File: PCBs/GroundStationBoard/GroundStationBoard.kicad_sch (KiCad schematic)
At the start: 4 parts, among them J1 SMA_CONNECTOR, U1 RFM98W

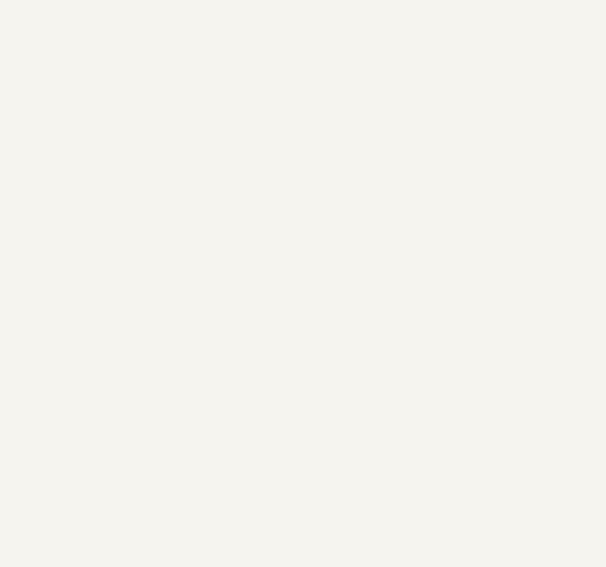
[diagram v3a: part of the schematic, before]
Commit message: added amplifier
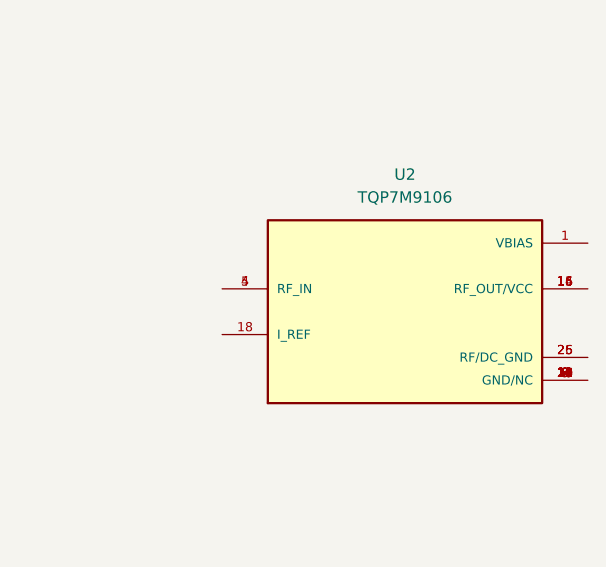
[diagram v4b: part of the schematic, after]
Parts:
- added U2: TQP7M9106, TQP7M9106:QFN50P400X400X90-25N, symbol TQP7M9106:TQP7M9106
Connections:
- new net: U2.10 (GND/NC), U2.11 (GND/NC), U2.12 (GND/NC), U2.13 (GND/NC), U2.17 (GND/NC), U2.19 (GND/NC), U2.2 (GND/NC), U2.20 (GND/NC), U2.21 (GND/NC), U2.22 (GND/NC), U2.23 (GND/NC), U2.24 (GND/NC), U2.3 (GND/NC), U2.6 (GND/NC), U2.7 (GND/NC), U2.8 (GND/NC), U2.9 (GND/NC)
- new net: U2.14 (RF_OUT/VCC), U2.15 (RF_OUT/VCC), U2.16 (RF_OUT/VCC)
- new net: U2.25 (RF/DC_GND), U2.26 (RF/DC_GND)
- new net: U2.4 (RF_IN), U2.5 (RF_IN)
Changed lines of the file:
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@@
     (pin "1")
+  )
+  (symbol (lib_id "TQP7M9106:TQP7M9106") (at 234.95 95.25 0) (unit 1)
+    (in_bom yes) (on_board yes) (fields_autoplaced)
+    (property "Reference" "U2" (id 0) (at 234.95 80.01 0))
+    (property "Value" "TQP7M9106" (id 1) (at 234.95 82.55 0))
+    (property "Footprint" "TQP7M9106:QFN50P400X400X90-25N" (id 2) (at 234.95 95.25 0)
+      (effects (font (size 1.27 1.27)) (justify left bottom) hide)
+    )
+    (property "Datasheet" "" (id 3) (at 234.95 95.25 0)
+      (effects (font (size 1.27 1.27)) (justify left bottom) hide)
+    )
+    (property "MANUFACTURER" "Qorvo" (id 4) (at 234.95 95.25 0)
+      (effects (font (size 1.27 1.27)) (justify left bottom) hide)
+    )
+    (property "STANDARD" "IPC-7351B" (id 5) (at 234.95 95.25 0)
+      (effects (font (size 1.27 1.27)) (justify left bottom) hide)
+    )
+    (property "SNAPEDA_PN" "TQP7M9106" (id 6) (at 234.95 95.25 0)
+      (effects (font (size 1.27 1.27)) (justify left bottom) hide)
+    )
+    (property "PARTREV" "Rev.D" (id 7) (at 234.95 95.25 0)
+      (effects (font (size 1.27 1.27)) (justify left bottom) hide)
+    )
+    (property "MAXIMUM_PACKAGE_HEIGHT" "0.9 mm" (id 8) (at 234.95 95.25 0)
+      (effects (font (size 1.27 1.27)) (justify left bottom) hide)
+    )
+    (pin "1")
+    (pin "10")
+    (pin "11")
+    (pin "12")
+    (pin "13")
+    (pin "14")
+    (pin "15")
+    (pin "16")
+    (pin "17")
+    (pin "18")
+    (pin "19")
+    (pin "2")
+    (pin "20")
+    (pin "21")
+    (pin "22")
+    (pin "23")
+    (pin "24")
+    (pin "25")
+    (pin "26")
+    (pin "3")
+    (pin "4")
+    (pin "5")
+    (pin "6")
+    (pin "7")
+    (pin "8")
+    (pin "9")
   )
   (symbol (lib_id "power:GND") (at 111.76 63.5 0) (unit 1)
@@
   (symbol (lib_id "power:GND") (at 152.4 114.3 0) (unit 1)
     (in_bom yes) (on_board yes)
-    (property "Reference" "#PWR016" (id 0) (at 152.4 120.65 0)
+    (property "Reference" "#PWR013" (id 0) (at 152.4 120.65 0)
       (effects (font (size 1.27 1.27)) hide)
     )
@@
       (reference "#PWR012") (unit 1) (value "GND") (footprint "")
     )
+    (path "/d773327a-e8d6-4108-a114-a6c62372afcb"
+      (reference "#PWR013") (unit 1) (value "GND") (footprint "")
+    )
     (path "/df933423-8150-4da9-a8c1-053c01a26516"
       (reference "#PWR014") (unit 1) (value "+3.3V") (footprint "")
@@
       (reference "#PWR015") (unit 1) (value "GND") (footprint "")
     )
-    (path "/d773327a-e8d6-4108-a114-a6c62372afcb"
-      (reference "#PWR016") (unit 1) (value "GND") (footprint "")
-    )
     (path "/695f3645-22ae-40bc-a3f8-3d3b654779fc"
       (reference "A1") (unit 1) (value "Raspberry Pi Zero") (footprint "ADA3708:ADA3708_RPI-ZERO")
@@
       (reference "U1") (unit 1) (value "RFM98W") (footprint "RFM98W-433S2:XCVR_RFM98W-433S2")
     )
-  )
+    (path "/6e9a568d-d4c1-4c8f-ab20-c2e09c01ec01"
+      (reference "U2") (unit 1) (value "TQP7M9106") (footprint "TQP7M9106:QFN50P400X400X90-25N")
+    )
+  )

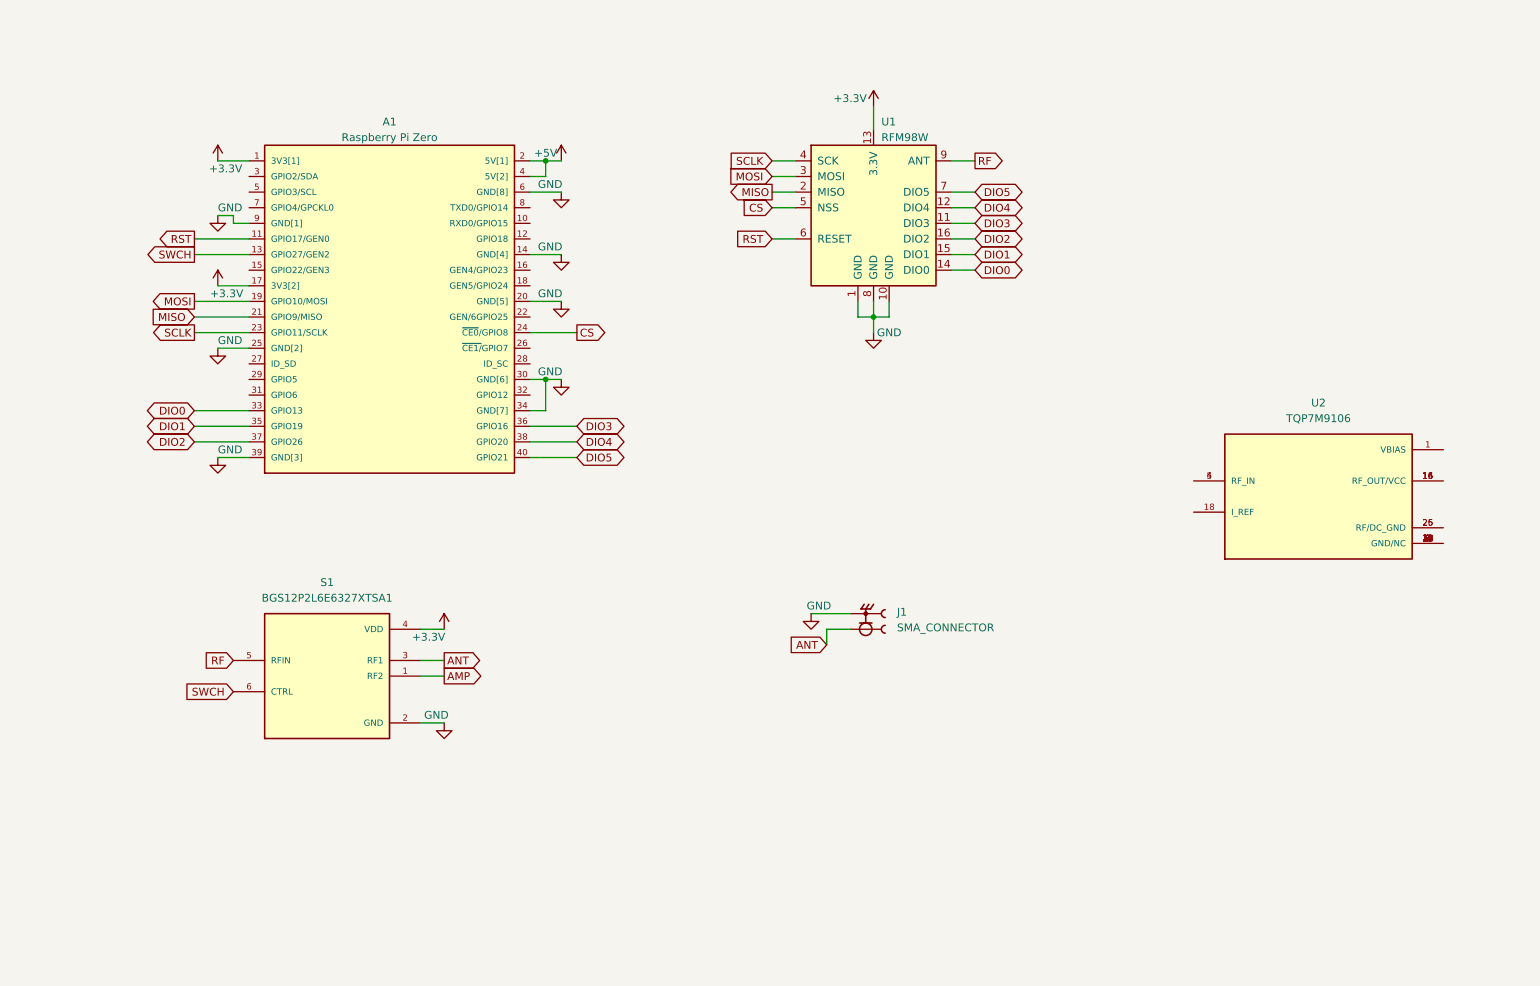
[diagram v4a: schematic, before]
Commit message: decoupling capacitors & amplifier
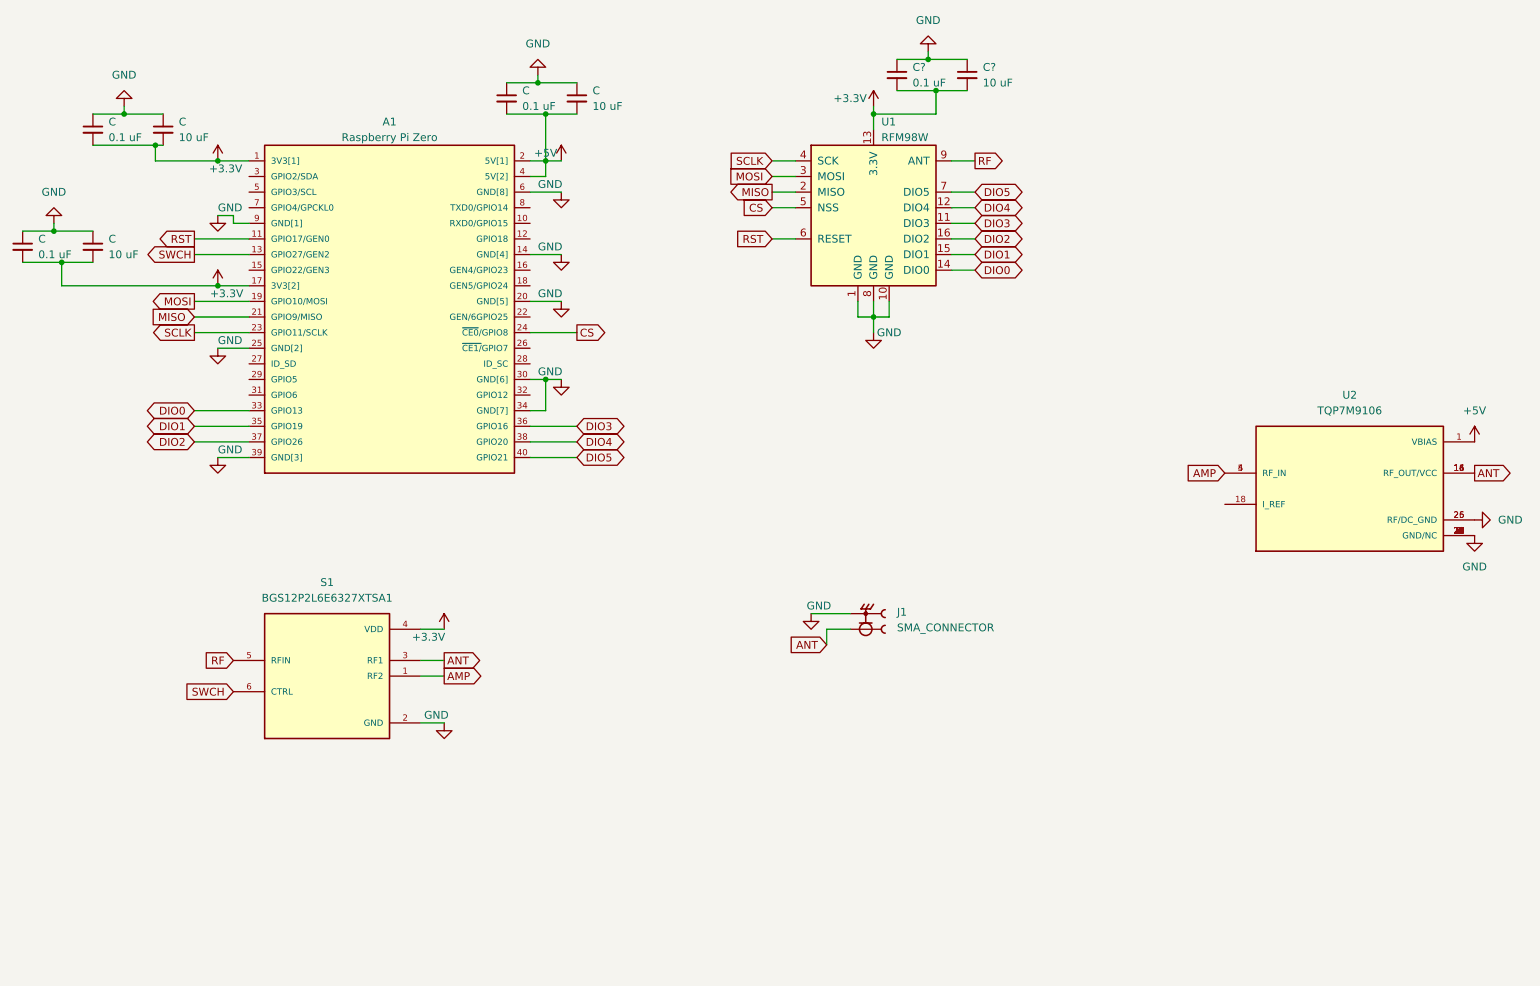
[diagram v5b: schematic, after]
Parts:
- added C (x3), C?: 0.1 uF, symbol Device:C_Small
- added C (x3), C?: 10 uF, symbol Device:C_Small
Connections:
- net +3.3V: now also C.2, C.2, C.2, C.2, C?.2, C?.2
- net +5V: now also U2.1 (VBIAS), C.2, C.2
- net AMP: now also U2.4 (RF_IN), U2.5 (RF_IN)
- net ANT: now also U2.14 (RF_OUT/VCC), U2.15 (RF_OUT/VCC), U2.16 (RF_OUT/VCC)
- net GND: now also U2.10 (GND/NC), U2.11 (GND/NC), U2.12 (GND/NC), U2.13 (GND/NC), U2.17 (GND/NC), U2.19 (GND/NC), U2.2 (GND/NC), U2.20 (GND/NC), U2.21 (GND/NC), U2.22 (GND/NC), U2.23 (GND/NC), U2.24 (GND/NC), U2.25 (RF/DC_GND), U2.26 (RF/DC_GND), U2.3 (GND/NC), U2.6 (GND/NC), U2.7 (GND/NC), U2.8 (GND/NC), U2.9 (GND/NC), C.1, C.1, C.1, C.1, C.1, C.1, C?.1, C?.1
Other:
- moved on the sheet: U2
